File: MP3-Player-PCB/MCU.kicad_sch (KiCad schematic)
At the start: 15 parts, among them J101 Conn_ARM_SWD_TagConnect_TC2030, U101 STM32F411CEUx, Y101 8MHz

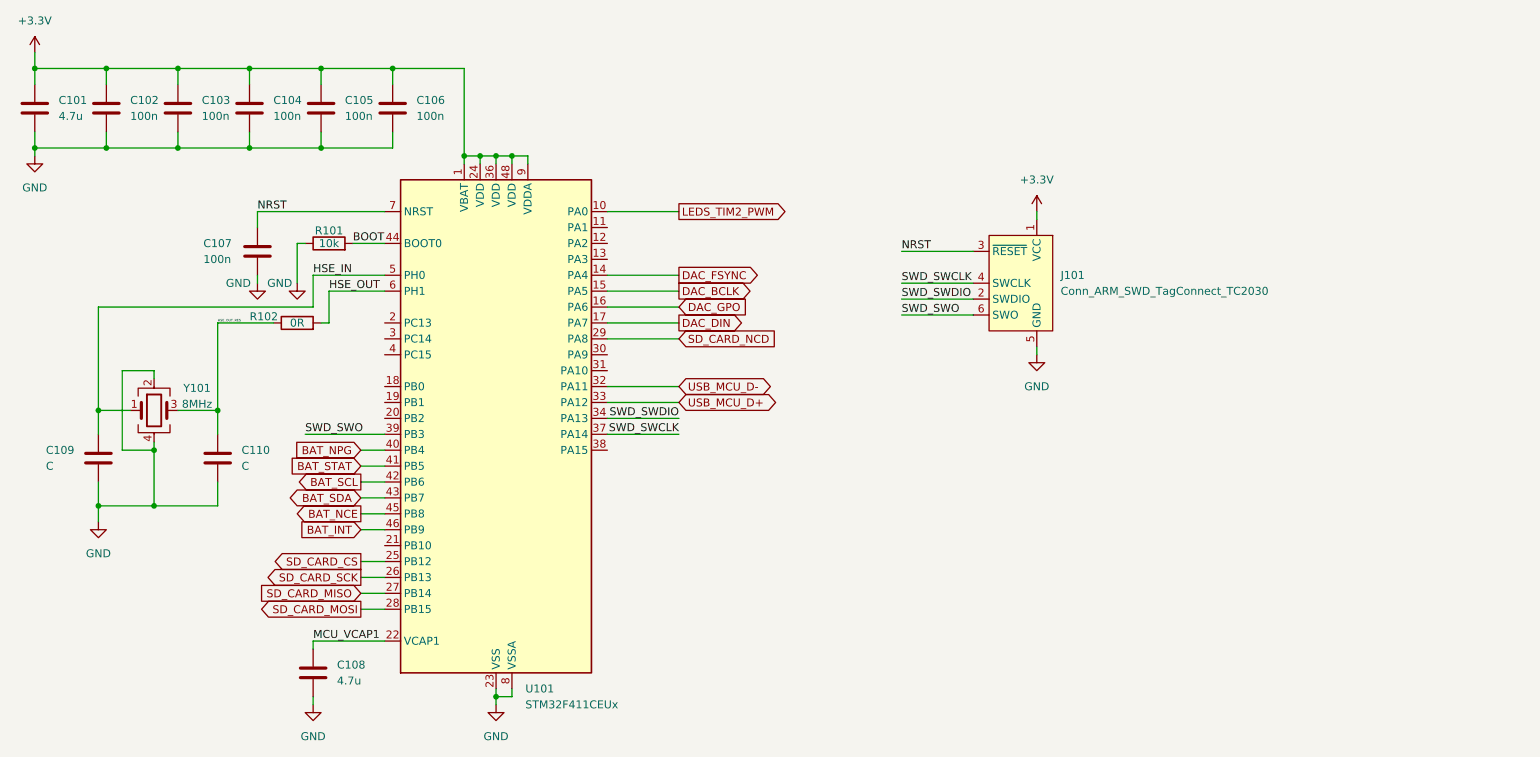
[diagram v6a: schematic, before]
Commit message: Added button circuitry
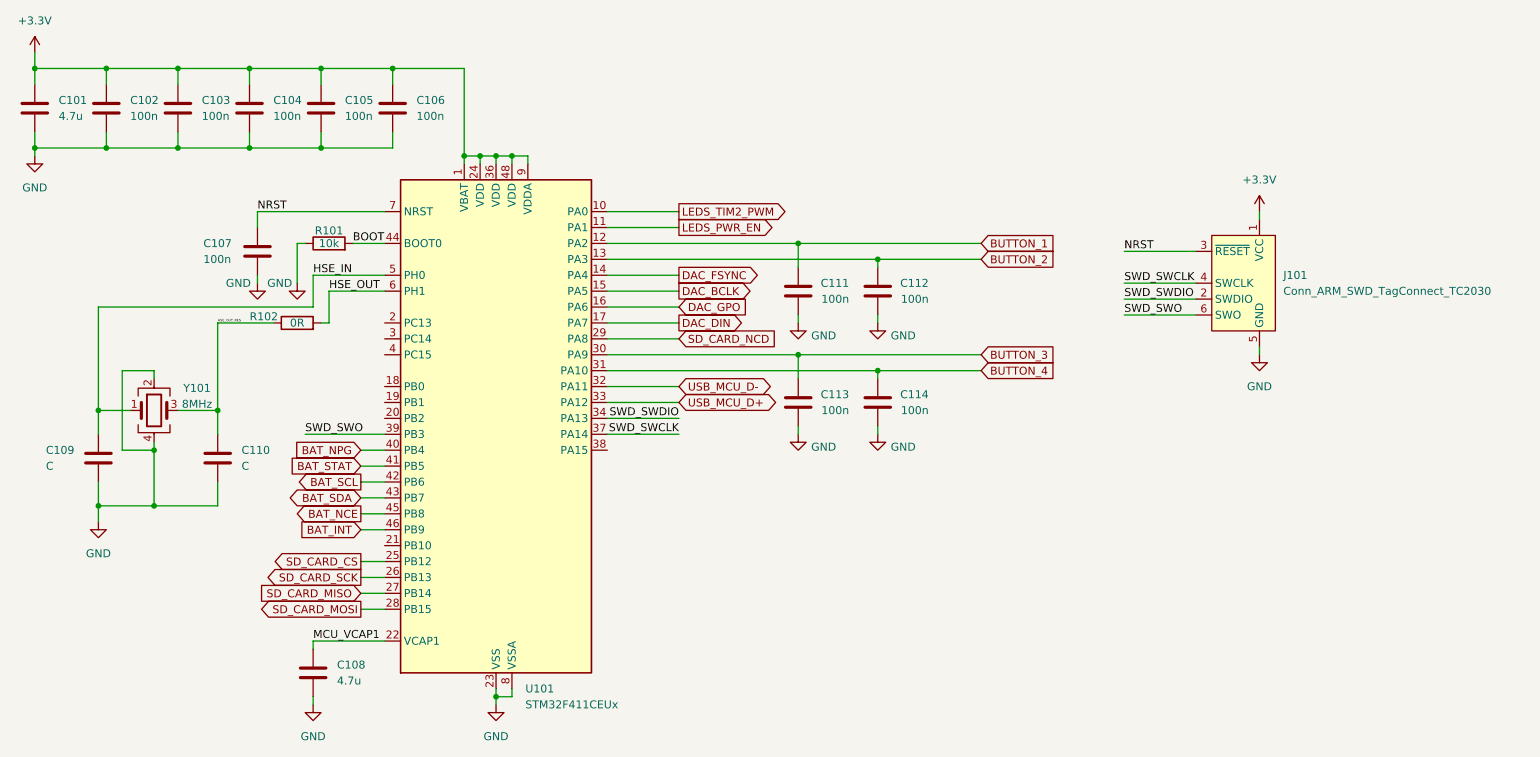
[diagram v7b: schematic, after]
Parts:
- added C111, C112, C113, C114: 100n, symbol Device:C
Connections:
- net GND: now also C111.2, C112.2, C113.2, C114.2
- net LEDS_PWR_EN: now reaches U101.11 (PA1)
- net BUTTON_1: now reaches U101.12 (PA2)
- net BUTTON_1: now also C111.1
- net BUTTON_2: now reaches U101.13 (PA3)
- net BUTTON_2: now also C112.1
- net BUTTON_3: now reaches U101.30 (PA9)
- net BUTTON_3: now also C113.1
- net BUTTON_4: now reaches U101.31 (PA10)
- net BUTTON_4: now also C114.1
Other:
- moved on the sheet: J101

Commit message: Added esd protection to audiojack and sd card. Also added jack detection on audiojack
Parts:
- renumbered C111 to C108, C112 to C109, C113 to C110, C114 to C111, C109 to C112, C110 to C113, C108 to C114
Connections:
- net AUDIO_JACK_DET: now reaches U101.38 (PA15)
- no-connect marks 0 -> 7
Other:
- moved on the sheet: C108, C109, C110, C111
